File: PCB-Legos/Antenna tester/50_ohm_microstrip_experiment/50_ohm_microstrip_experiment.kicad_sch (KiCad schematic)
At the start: 9 parts, among them J1 Conn_Coaxial, J3 Conn_Coaxial, J4 Conn_Coaxial, J5 Conn_Coaxial

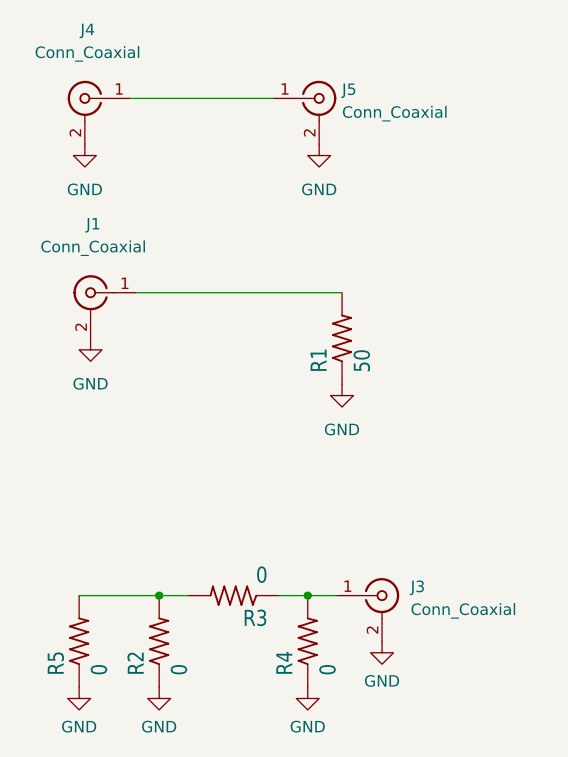
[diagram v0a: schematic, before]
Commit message: Update with open stub/ changes
-Added vias, removed DNP components, moved components closer together
- implemented open stub experiment
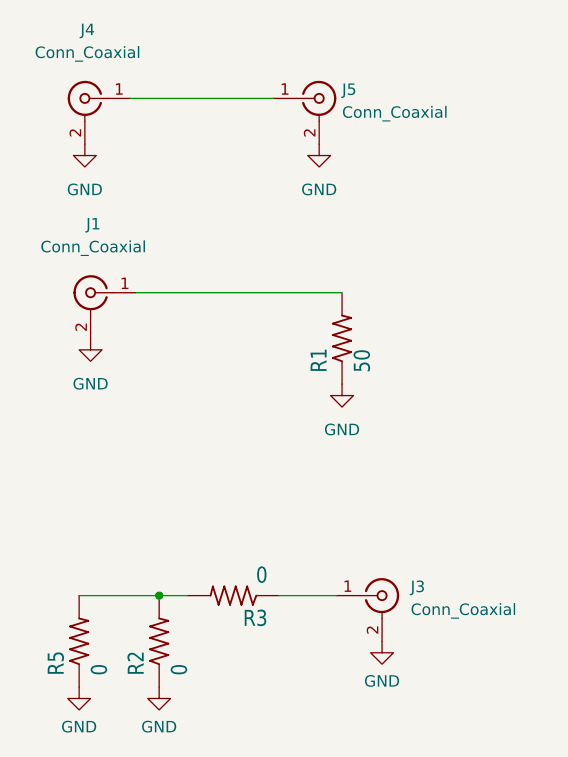
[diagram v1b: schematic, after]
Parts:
- removed R4: 0, HGS_Reflector:.0402-C-NOSILK, symbol HGS_Reflector-eagle-import:R-US_0603-B-NOSILK
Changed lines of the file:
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@@
   (junction (at 107.95 125.095) (diameter 0) (color 0 0 0 0)
   )
-  (junction (at 124.46 125.095) (diameter 0) (color 0 0 0 0)
-  )
   (wire (pts (xy 107.95 125.095) (xy 111.125 125.095))
     (stroke (width 0) (type default) (color 0 0 0 0))
@@
     (stroke (width 0) (type default) (color 0 0 0 0))
   )
-  (wire (pts (xy 124.46 125.095) (xy 127.635 125.095))
-    (stroke (width 0) (type default) (color 0 0 0 0))
-  )
   (wire (pts (xy 104.775 69.85) (xy 120.65 69.85))
     (stroke (width 0) (type default) (color 0 0 0 0))
@@
     (stroke (width 0) (type default) (color 0 0 0 0))
   )
-  (wire (pts (xy 121.285 125.095) (xy 124.46 125.095))
-    (stroke (width 0) (type default) (color 0 0 0 0))
-  )
-  (symbol (lib_id "HGS_Reflector-eagle-import:R-US_0603-B-NOSILK") (at 124.46 130.175 90) (unit 1)
-    (in_bom yes) (on_board yes)
-    (property "Reference" "R4" (id 0) (at 122.9614 133.985 0)
-      (effects (font (size 1.778 1.5113)) (justify left bottom))
-    )
-    (property "Value" "0" (id 1) (at 127.762 133.985 0)
-      (effects (font (size 1.778 1.5113)) (justify left bottom))
-    )
-    (property "Footprint" "HGS_Reflector:.0402-C-NOSILK" (id 2) (at 124.46 130.175 0)
-      (effects (font (size 1.27 1.27)) hide)
-    )
-    (property "Datasheet" "" (id 3) (at 124.46 130.175 0)
-      (effects (font (size 1.27 1.27)) hide)
-    )
-    (pin "1")
-    (pin "2")
+  (wire (pts (xy 121.285 125.095) (xy 127.635 125.095))
+    (stroke (width 0) (type default) (color 0 0 0 0))
   )
   (symbol (lib_id "power:GND") (at 100.33 96.52 0) (unit 1)
@@
     (pin "2")
   )
-  (symbol (lib_id "power:GND") (at 124.46 135.255 0) (unit 1)
-    (in_bom yes) (on_board yes) (fields_autoplaced)
-    (property "Reference" "#PWR0105" (id 0) (at 124.46 141.605 0)
-      (effects (font (size 1.27 1.27)) hide)
-    )
-    (property "Value" "GND" (id 1) (at 124.46 139.7 0))
-    (property "Footprint" "" (id 2) (at 124.46 135.255 0)
-      (effects (font (size 1.27 1.27)) hide)
-    )
-    (property "Datasheet" "" (id 3) (at 124.46 135.255 0)
-      (effects (font (size 1.27 1.27)) hide)
-    )
-    (pin "1")
-  )
   (symbol (lib_id "Connector:Conn_Coaxial") (at 100.33 91.44 0) (mirror y) (unit 1)
     (in_bom yes) (on_board yes) (fields_autoplaced)
@@
       (reference "#PWR0104") (unit 1) (value "GND") (footprint "")
     )
-    (path "/69afbd89-c2dd-4bfe-9ebc-4b30825928d1"
-      (reference "#PWR0105") (unit 1) (value "GND") (footprint "")
-    )
     (path "/97e0d8f2-3fb5-4132-bc5b-5e7a03ef2bdb"
       (reference "#PWR0106") (unit 1) (value "GND") (footprint "")
@@
       (reference "R3") (unit 1) (value "0") (footprint "HGS_Reflector:.0402-C-NOSILK")
     )
-    (path "/03a6503e-3bc6-4f20-910b-4b25d7b2c144"
-      (reference "R4") (unit 1) (value "0") (footprint "HGS_Reflector:.0402-C-NOSILK")
-    )
     (path "/3cbded9b-575b-4629-a1c2-e5f5a8f91c4a"

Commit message: Fixed vias and ground plane
moved some vias around and fixed the ground plane around the stub to follow the 3W rule.
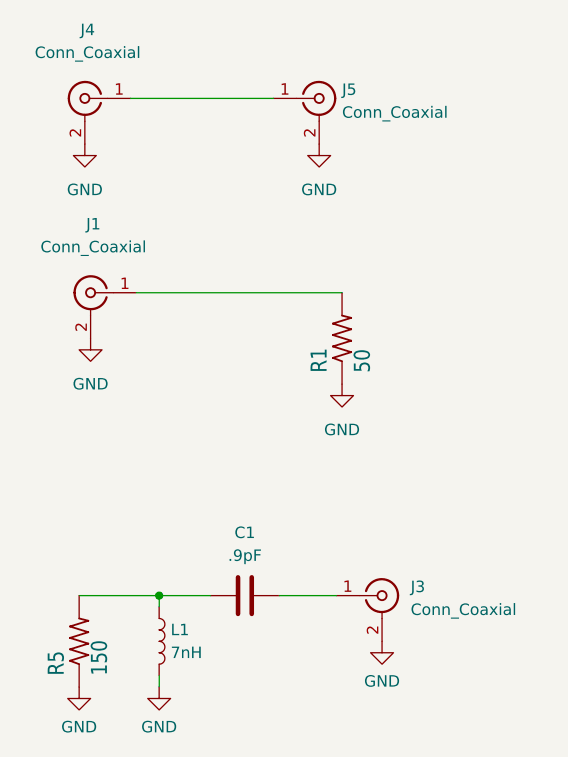
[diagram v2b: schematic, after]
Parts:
- removed R2, R3: 0, HGS_Reflector:.0402-C-NOSILK, symbol HGS_Reflector-eagle-import:R-US_0603-B-NOSILK
- added C1: .9pF, HGS_Reflector:.0402-C-NOSILK, symbol Device:C
- added L1: 7nH, HGS_Reflector:.0402-C-NOSILK, symbol Device:L
- R5: value 0 -> 150
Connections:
- net GND: now also L1.2
- net at R5.2: now also C1.1, L1.1
- net at J3.1 (In): now also C1.2
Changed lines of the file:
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@@
   (junction (at 107.95 125.095) (diameter 0) (color 0 0 0 0)
   )
-  (wire (pts (xy 107.95 125.095) (xy 111.125 125.095))
+  (wire (pts (xy 107.95 125.095) (xy 107.95 126.365))
     (stroke (width 0) (type default) (color 0 0 0 0))
   )
@@
   )
   (wire (pts (xy 104.775 69.85) (xy 120.65 69.85))
+    (stroke (width 0) (type default) (color 0 0 0 0))
+  )
+  (wire (pts (xy 107.95 133.985) (xy 107.95 135.255))
+    (stroke (width 0) (type default) (color 0 0 0 0))
+  )
+  (wire (pts (xy 107.95 125.095) (xy 113.665 125.095))
     (stroke (width 0) (type default) (color 0 0 0 0))
   )
@@
       (effects (font (size 1.778 1.5113)) (justify left bottom))
     )
-    (property "Value" "0" (id 1) (at 102.362 133.985 0)
+    (property "Value" "150" (id 1) (at 102.362 133.985 0)
       (effects (font (size 1.778 1.5113)) (justify left bottom))
     )
@@
     (pin "2")
   )
-  (symbol (lib_id "HGS_Reflector-eagle-import:R-US_0603-B-NOSILK") (at 116.205 125.095 180) (unit 1)
-    (in_bom yes) (on_board yes)
-    (property "Reference" "R3" (id 0) (at 120.015 126.5936 0)
-      (effects (font (size 1.778 1.5113)) (justify left bottom))
-    )
-    (property "Value" "0" (id 1) (at 120.015 121.793 0)
-      (effects (font (size 1.778 1.5113)) (justify left bottom))
-    )
-    (property "Footprint" "HGS_Reflector:.0402-C-NOSILK" (id 2) (at 116.205 125.095 0)
-      (effects (font (size 1.27 1.27)) hide)
-    )
-    (property "Datasheet" "" (id 3) (at 116.205 125.095 0)
+  (symbol (lib_id "Device:L") (at 107.95 130.175 0) (unit 1)
+    (in_bom yes) (on_board yes) (fields_autoplaced)
+    (property "Reference" "L1" (id 0) (at 109.22 128.9049 0)
+      (effects (font (size 1.27 1.27)) (justify left))
+    )
+    (property "Value" "7nH" (id 1) (at 109.22 131.4449 0)
+      (effects (font (size 1.27 1.27)) (justify left))
+    )
+    (property "Footprint" "HGS_Reflector:.0402-C-NOSILK" (id 2) (at 107.95 130.175 0)
+      (effects (font (size 1.27 1.27)) hide)
+    )
+    (property "Datasheet" "~" (id 3) (at 107.95 130.175 0)
       (effects (font (size 1.27 1.27)) hide)
     )
@@
     (pin "1")
   )
-  (symbol (lib_id "HGS_Reflector-eagle-import:R-US_0603-B-NOSILK") (at 107.95 130.175 90) (unit 1)
-    (in_bom yes) (on_board yes)
-    (property "Reference" "R2" (id 0) (at 106.4514 133.985 0)
-      (effects (font (size 1.778 1.5113)) (justify left bottom))
-    )
-    (property "Value" "0" (id 1) (at 111.252 133.985 0)
-      (effects (font (size 1.778 1.5113)) (justify left bottom))
-    )
-    (property "Footprint" "HGS_Reflector:.0402-C-NOSILK" (id 2) (at 107.95 130.175 0)
-      (effects (font (size 1.27 1.27)) hide)
-    )
-    (property "Datasheet" "" (id 3) (at 107.95 130.175 0)
-      (effects (font (size 1.27 1.27)) hide)
-    )
-    (pin "1")
-    (pin "2")
-  )
   (symbol (lib_id "Connector:Conn_Coaxial") (at 125.73 69.85 0) (unit 1)
     (in_bom yes) (on_board yes) (fields_autoplaced)
@@
     )
     (property "M/N" "142-0701-806" (id 4) (at 99.695 69.85 0)
+      (effects (font (size 1.27 1.27)) hide)
+    )
+    (pin "1")
+    (pin "2")
+  )
+  (symbol (lib_id "Device:C") (at 117.475 125.095 90) (unit 1)
+    (in_bom yes) (on_board yes) (fields_autoplaced)
+    (property "Reference" "C1" (id 0) (at 117.475 118.11 90))
+    (property "Value" ".9pF" (id 1) (at 117.475 120.65 90))
+    (property "Footprint" "HGS_Reflector:.0402-C-NOSILK" (id 2) (at 121.285 124.1298 0)
+      (effects (font (size 1.27 1.27)) hide)
+    )
+    (property "Datasheet" "~" (id 3) (at 117.475 125.095 0)
       (effects (font (size 1.27 1.27)) hide)
     )
@@
       (reference "#PWR0108") (unit 1) (value "GND") (footprint "")
     )
+    (path "/e25f0cb2-d101-4680-8039-e28dc3ef0e9b"
+      (reference "C1") (unit 1) (value ".9pF") (footprint "HGS_Reflector:.0402-C-NOSILK")
+    )
     (path "/7b2e7361-0d1f-4a92-a4d0-dd4722c9bc0c"
       (reference "J1") (unit 1) (value "Conn_Coaxial") (footprint "Cinch:CONN_142-0701-851_CIN")
@@
       (reference "J5") (unit 1) (value "Conn_Coaxial") (footprint "Cinch:CONN_142-0701-851_CIN")
     )
+    (path "/488ff63f-1512-4eec-9188-185416b28e19"
+      (reference "L1") (unit 1) (value "7nH") (footprint "HGS_Reflector:.0402-C-NOSILK")
+    )
     (path "/f87e64da-fa0c-4b2c-994b-7de507d5096f"
       (reference "R1") (unit 1) (value "50") (footprint "HGS_Reflector:.0402-C-NOSILK")
     )
-    (path "/9d221b3b-0bfe-4439-a426-0f2594b9c7bf"
-      (reference "R2") (unit 1) (value "0") (footprint "HGS_Reflector:.0402-C-NOSILK")
-    )
-    (path "/53ded23b-dad2-4c6d-9d77-91fa13f8ed66"
-      (reference "R3") (unit 1) (value "0") (footprint "HGS_Reflector:.0402-C-NOSILK")
-    )
     (path "/3cbded9b-575b-4629-a1c2-e5f5a8f91c4a"
-      (reference "R5") (unit 1) (value "0") (footprint "HGS_Reflector:.0402-C-NOSILK")
-    )
-  )
+      (reference "R5") (unit 1) (value "150") (footprint "HGS_Reflector:.0402-C-NOSILK")
+    )
+  )
